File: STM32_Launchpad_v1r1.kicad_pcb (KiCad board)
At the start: 4 copper layers, 54 x 75 mm, 61 parts, among them J1 Conn_01x04, J2 USB_B_Micro, J3 Conn_02x10_Counter_Clockwise, J4 Conn_01x02, J5 Conn_02x10_Counter_Clockwise, J6 Conn_01x03, J7 Conn_02x03_Odd_Even, J8 Conn_01x02, SW1 SW_Push, U1 TPD2EUSB30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

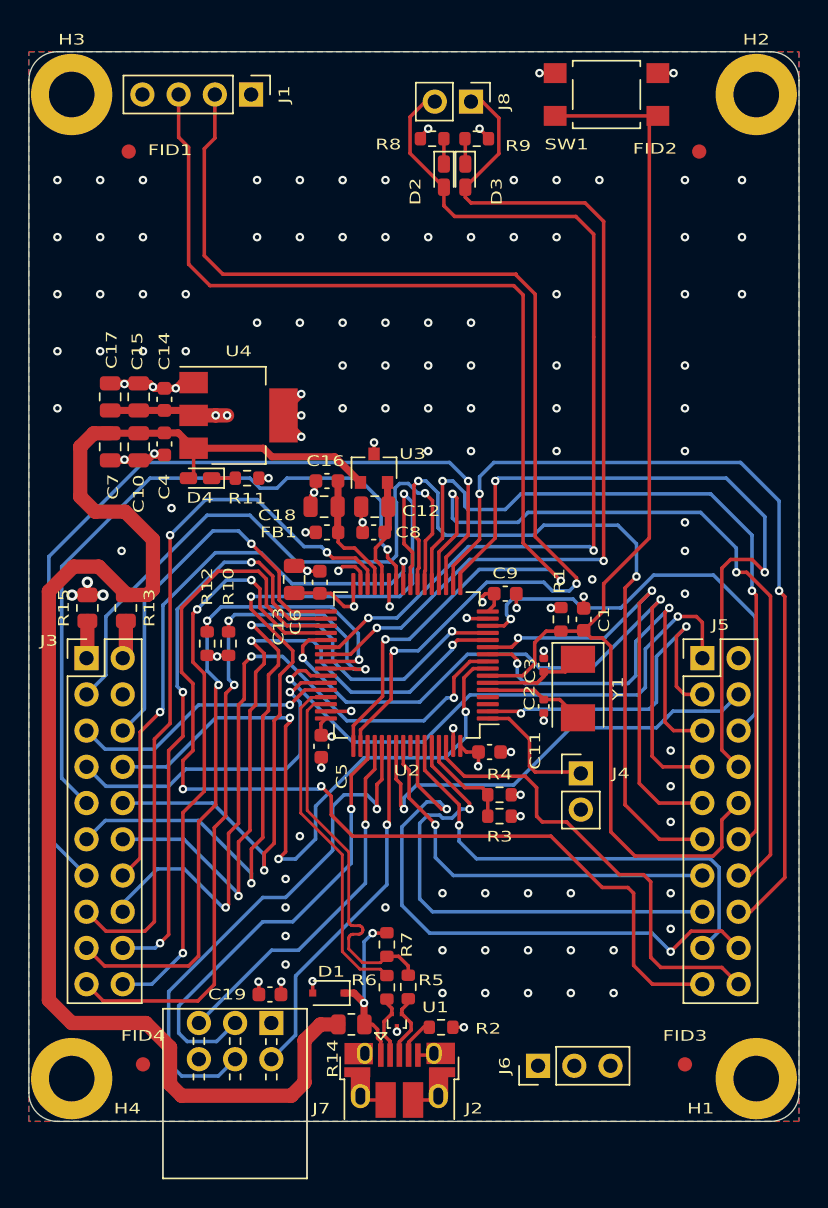
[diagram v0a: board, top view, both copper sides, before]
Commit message: Updated and improved pin arrangement
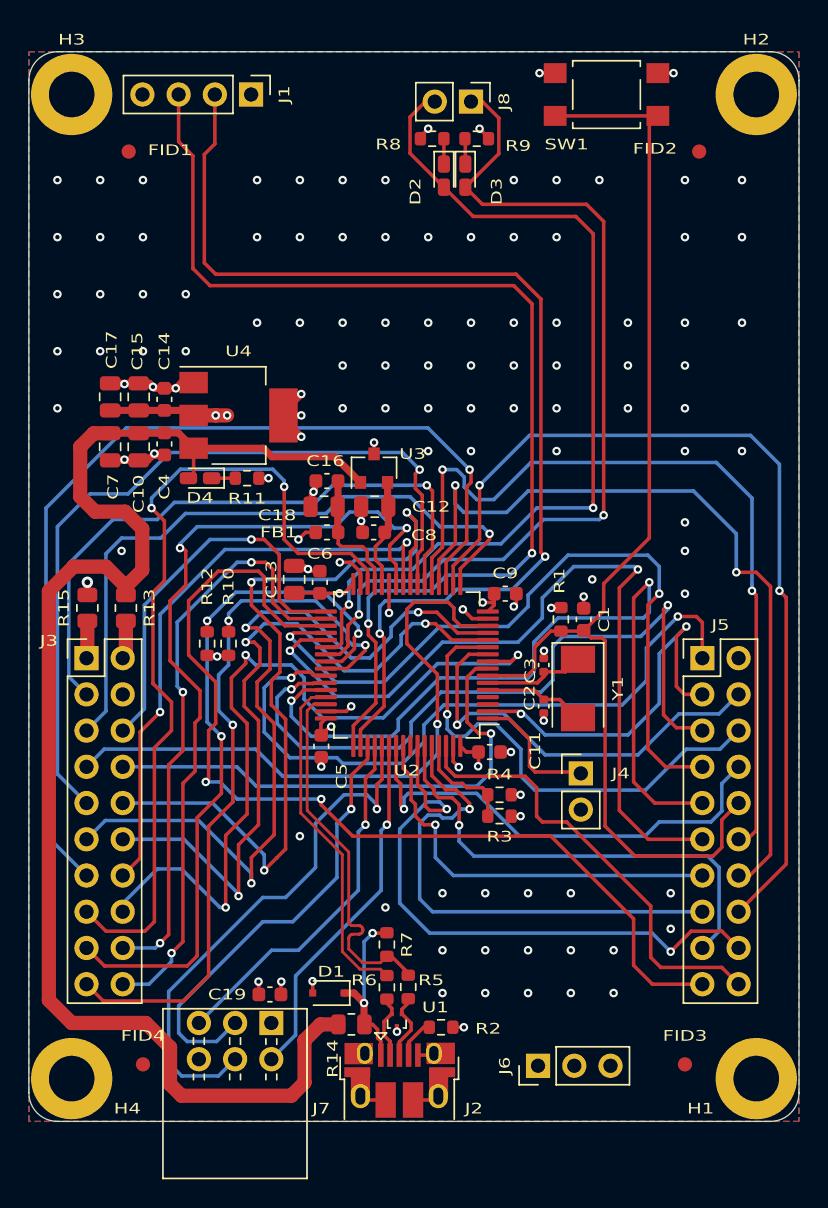
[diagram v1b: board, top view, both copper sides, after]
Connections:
- J3 pad 20: /PB14_AD4 -> /PB2_AD2
- J5 pad 4: /GPIO\EI1 -> /GPIO\EI3
- J5 pad 6: /GPIO\EI3 -> /GPIO\EI4
- J5 pad 8: /GPIO\EI4 -> /GPIO\EI1
- U2 pad 10: /PWMBH -> /GPIO\EI3
- U2 pad 11: /PWMCH -> /GPIO\EI4
- U2 pad 14: /GPIO\EI3 -> /UART_MCUTX
- U2 pad 17: /GPIO\EI4 -> /UART_MCURX
- U2 pad 23: /PWMCL -> /GPIO\EI5
- U2 pad 26: /GPIO\EI5 -> /PB2_AD2
- U2 pad 36: /PB14_AD4 -> /PWMBL
- U2 pad 37: /PWMBL -> /PWMCL
- U2 pad 43: /UART_MCUTX -> /PWMBH
- U2 pad 44: /UART_MCURX -> /PWMCH
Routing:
- net /PB2_AD2: track 0.00 -> 57.7 mm, vias 0 -> 3
- net /PB14_AD4: track 42.8 -> 0.00 mm, vias 3 -> 0
- net /UART_MCURX: track 19.0 -> 47.0 mm
- net /PWMCH: track 32.1 -> 56.8 mm
- net /PWMBH: track 28.8 -> 51.3 mm
- net /UART_MCUTX: track 24.0 -> 44.6 mm
- net /GPIO\EI4: track 50.3 -> 34.0 mm, vias 2 -> 1
- net /PC0_AD2: track 47.6 -> 36.3 mm, vias 3 -> 1
- net /GPIO\EI6: track 51.1 -> 59.4 mm
- net /PWMAH: track 41.6 -> 48.7 mm
- net /GPIO\EI5: track 49.8 -> 56.8 mm
- net /PC1_AD2: track 49.3 -> 55.0 mm
- net /PWMCL: track 51.7 -> 57.3 mm
- net /SPISCK: track 64.0 -> 69.0 mm
- net /PWMBL: track 47.9 -> 51.8 mm
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
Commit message: Added silkscreen header markings
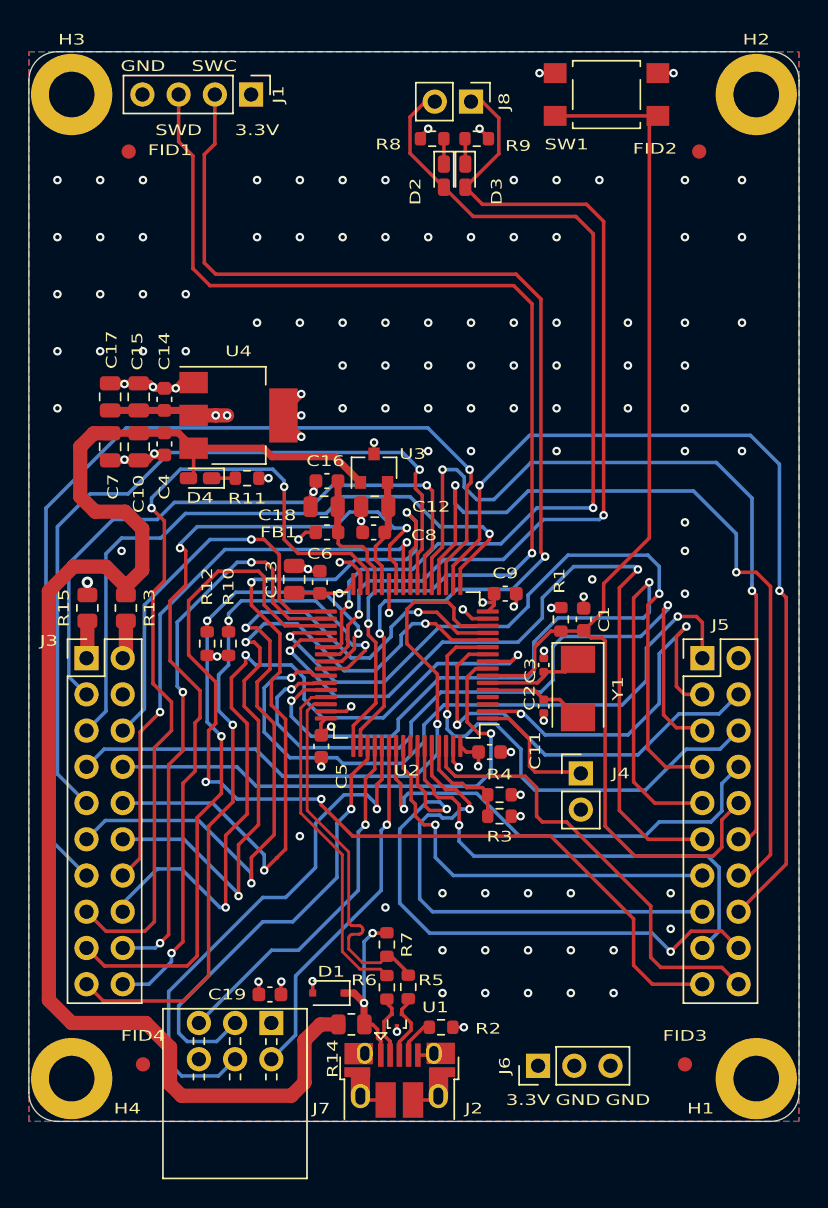
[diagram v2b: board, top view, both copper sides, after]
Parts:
- added REF**: OSHW-Symbol_6.7x6mm_SilkScreen, Symbol:OSHW-Symbol_6.7x6mm_SilkScreen, B.Cu at (87.5, 78.0)
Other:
- board text added: "3.3V"
- board text added: "5V"
- board text added: "AD1I1"
- board text added: "AD1I14"
- board text added: "AD1I2"
- board text added: "AD2I12"
- board text added: "AD2I5"
- board text added: "AD2I6"
- board text added: "AD2I7"
- board text added: "AD3I1"
- board text added: "AD3I12"
- board text added: "AD4I3"
- board text added: "CANRX"
- board text added: "CANTX"
- board text added: "ENCA"
- board text added: "ENCB"
- board text added: "ENCZ"
- board text added: "GIO1"
- board text added: "GIO2"
- board text added: "GIO3"
- board text added: "GIO4"
- board text added: "GIO5"
- board text added: "GIO6"
- board text added: "GND"
- board text added: "I2CCL"
- board text added: "I2CDA"
- board text added: "PWMAH"
- board text added: "PWMAL"
- board text added: "PWMBH"
- board text added: "PWMBL"
- board text added: "PWMCH"
- board text added: "PWMCL"
- board text added: "RX"
- board text added: "SPICK"
- board text added: "SPIMI"
- board text added: "SPIMO"
- board text added: "SWC"
- board text added: "SWD"
- board text added: "TX"
- board text added: "~RST"
- board text added: "~SPICS"
